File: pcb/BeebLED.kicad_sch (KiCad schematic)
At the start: 13 parts, among them J1 BBC User Port, J2 Jack-DC, U1 74HC14, U2 74LS165, X1 8Mhz

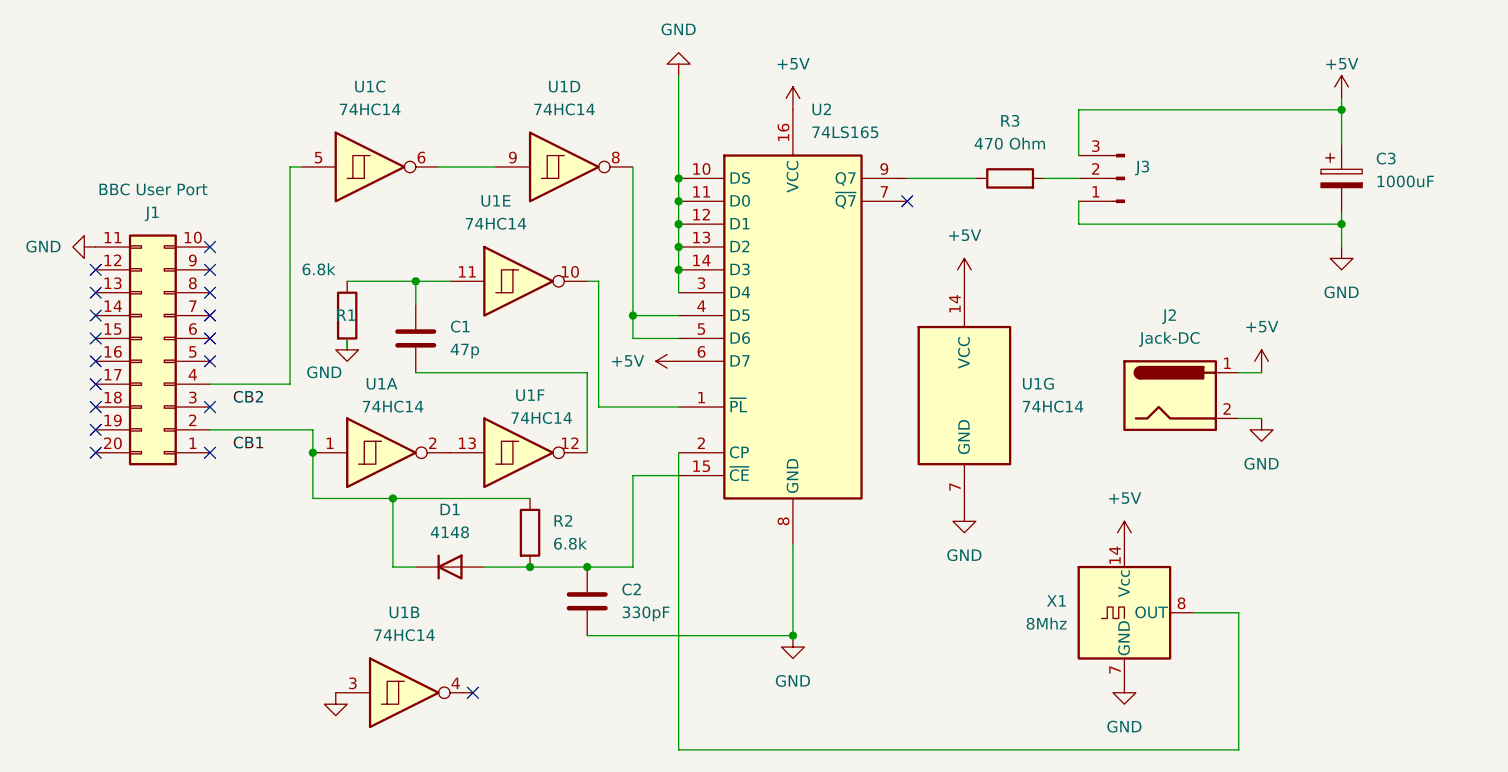
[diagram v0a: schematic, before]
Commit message: Added support for DIP8 crystal
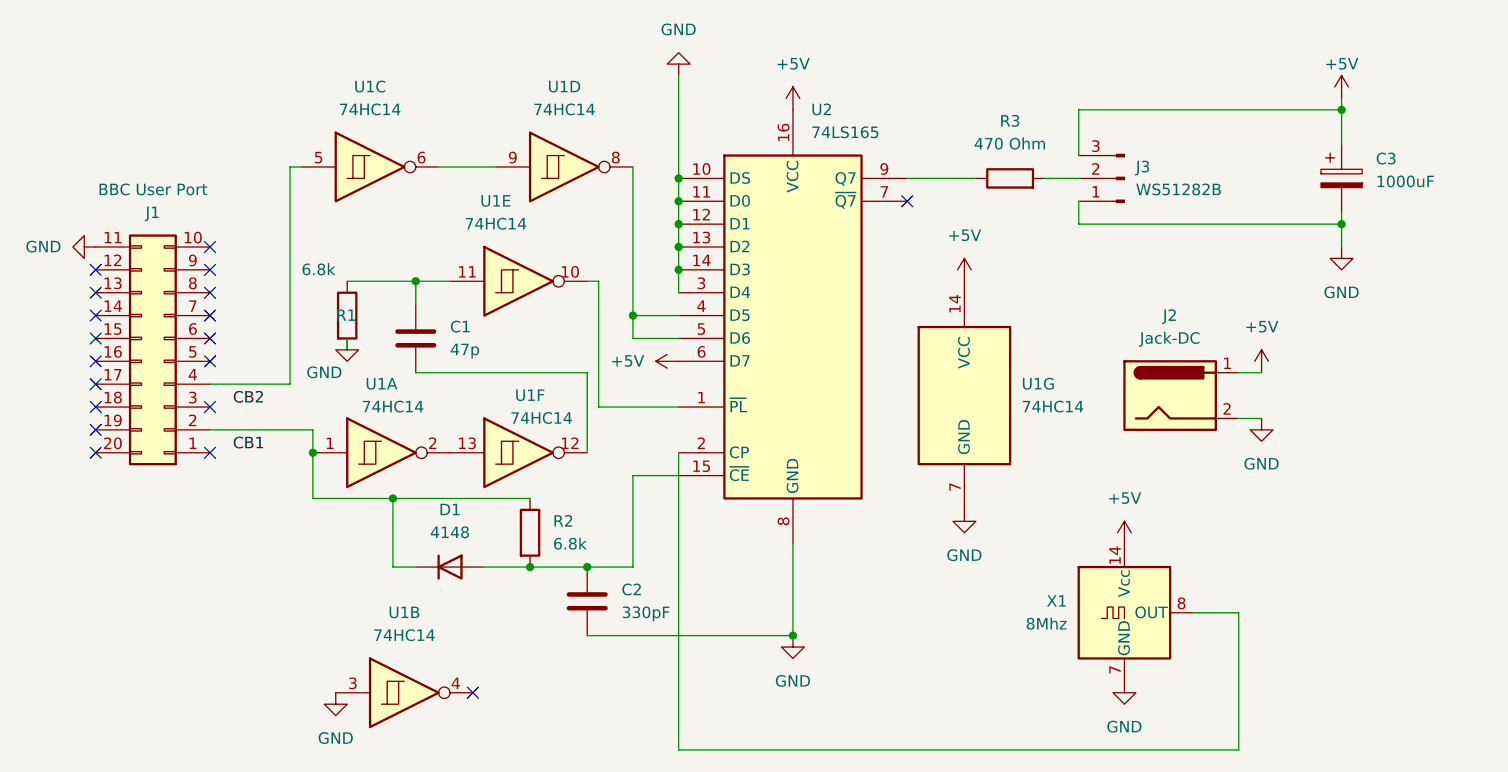
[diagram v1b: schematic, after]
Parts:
- J3: value (none) -> WS51282B; footprint (none) -> Connector_JST:JST_PH_S3B-PH-K_1x03_P2.00mm_Horizontal
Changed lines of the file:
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@@
       (effects (font (size 1.27 1.27)) hide)
     )
-    (property "Value" "" (id 1) (at 102.87 138.43 0))
+    (property "Value" "GND" (id 1) (at 102.87 138.43 0))
     (property "Footprint" "" (id 2) (at 102.87 133.35 0)
       (effects (font (size 1.27 1.27)) hide)
@@
       (effects (font (size 1.27 1.27)) (justify right))
     )
-    (property "Value" "" (id 1) (at 191.77 77.4699 0)
+    (property "Value" "WS51282B" (id 1) (at 191.77 77.4699 0)
       (effects (font (size 1.27 1.27)) (justify right))
     )
-    (property "Footprint" "" (id 2) (at 190.5 76.2 0)
-      (effects (font (size 1.27 1.27)) hide)
-    )
+    (property "Footprint" "Connector_JST:JST_PH_S3B-PH-K_1x03_P2.00mm_Horizontal" (id 2) (at 190.5 76.2 0)
+      (effects (font (size 1.27 1.27)) hide)
+    )

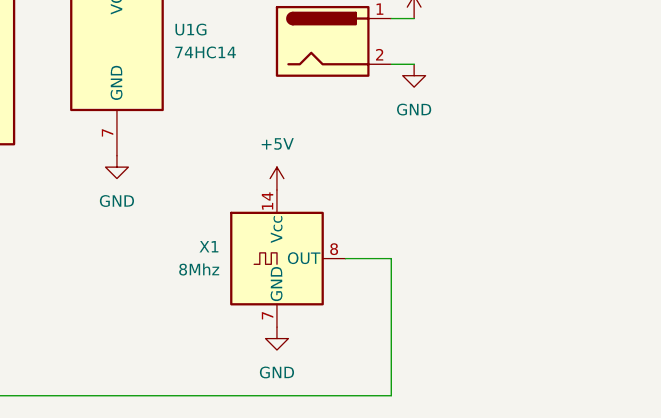
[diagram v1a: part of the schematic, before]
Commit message: Added alternative X2 component to schema and updated PCB
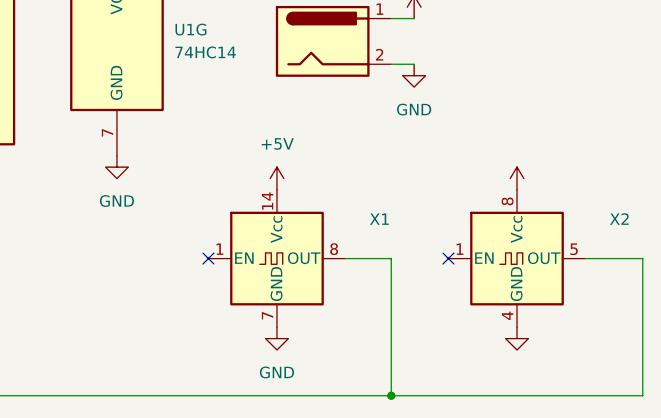
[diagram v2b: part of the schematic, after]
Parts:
- removed X1: 8Mhz, Oscillator:Oscillator_DIP-14, symbol Oscillator:DGOF5S3
- added X1: (no value), symbol Oscillator:CXO_DIP14
- added X2: (no value), symbol Oscillator:CXO_DIP8
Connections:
- net +5V: now also X1.14 (Vcc), X2.8 (Vcc)
- net GND: now also X1.7 (GND), X2.4 (GND)
- net at U2.2 (CP): now also X1.8 (OUT), X2.5 (OUT)
- no-connect marks 19 -> 21
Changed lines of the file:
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@@
   (title_block
     (title "BeebLed")
-    (date "2023-05-05")
-    (rev "v1.0")
+    (date "2023-05-07")
+    (rev "v1.1")
     (company "!FOZ!")
     (comment 1 "Derived from a design on ABNIELSEN.COM")
   )
+  (junction (at 203.2 139.7) (diameter 0) (color 0 0 0 0)
+  )
   (junction (at 100.33 106.68) (diameter 0) (color 0 0 0 0)
   )
@@
   (junction (at 140.97 78.74) (diameter 0) (color 0 0 0 0)
   )
+  (no_connect (at 182.88 124.46))
+  (no_connect (at 209.55 124.46))
   (no_connect (at 76.2 88.9))
   (no_connect (at 88.9 83.82))
@@
     (stroke (width 0) (type default) (color 0 0 0 0))
   )
+  (wire (pts (xy 231.14 124.46) (xy 231.14 139.7))
+    (stroke (width 0) (type default) (color 0 0 0 0))
+  )
   (wire (pts (xy 119.38 119.38) (xy 124.46 119.38))
     (stroke (width 0) (type default) (color 0 0 0 0))
@@
     (stroke (width 0) (type default) (color 0 0 0 0))
   )
+  (wire (pts (xy 203.2 139.7) (xy 231.14 139.7))
+    (stroke (width 0) (type default) (color 0 0 0 0))
+  )
   (wire (pts (xy 140.97 64.77) (xy 140.97 76.2))
     (stroke (width 0) (type default) (color 0 0 0 0))
@@
   )
   (wire (pts (xy 214.63 83.82) (xy 214.63 81.28))
+    (stroke (width 0) (type default) (color 0 0 0 0))
+  )
+  (wire (pts (xy 224.79 124.46) (xy 231.14 124.46))
     (stroke (width 0) (type default) (color 0 0 0 0))
   )
@@
     (pin "7")
   )
+  (symbol (lib_id "Oscillator:CXO_DIP14") (at 190.5 124.46 0) (unit 1)
+    (in_bom yes) (on_board yes) (fields_autoplaced)
+    (property "Reference" "X1" (id 0) (at 201.93 120.1293 0))
+    (property "Value" "" (id 1) (at 201.93 122.6693 0))
+    (property "Footprint" "" (id 2) (at 201.93 133.35 0)
+      (effects (font (size 1.27 1.27)) hide)
+    )
+    (property "Datasheet" "http://cdn-reichelt.de/documents/datenblatt/B400/OSZI.pdf" (id 3) (at 187.96 124.46 0)
+      (effects (font (size 1.27 1.27)) hide)
+    )
+    (pin "1")
+    (pin "14")
+    (pin "7")
+    (pin "8")
+  )
   (symbol (lib_id "power:GND") (at 76.2 83.82 270) (unit 1)
     (in_bom yes) (on_board yes) (fields_autoplaced)
@@
     (pin "1")
   )
+  (symbol (lib_id "power:GND") (at 217.17 132.08 0) (unit 1)
+    (in_bom yes) (on_board yes) (fields_autoplaced)
+    (property "Reference" "#PWR?" (id 0) (at 217.17 138.43 0)
+      (effects (font (size 1.27 1.27)) hide)
+    )
+    (property "Value" "" (id 1) (at 217.17 137.16 0))
+    (property "Footprint" "" (id 2) (at 217.17 132.08 0)
+      (effects (font (size 1.27 1.27)) hide)
+    )
+    (property "Datasheet" "" (id 3) (at 217.17 132.08 0)
+      (effects (font (size 1.27 1.27)) hide)
+    )
+    (pin "1")
+  )
   (symbol (lib_id "Device:C") (at 111.76 93.98 0) (unit 1)
     (in_bom yes) (on_board yes) (fields_autoplaced)
@@
     (pin "7")
   )
+  (symbol (lib_id "power:+5V") (at 217.17 116.84 0) (unit 1)
+    (in_bom yes) (on_board yes) (fields_autoplaced)
+    (property "Reference" "#PWR?" (id 0) (at 217.17 120.65 0)
+      (effects (font (size 1.27 1.27)) hide)
+    )
+    (property "Value" "" (id 1) (at 217.17 111.76 0))
+    (property "Footprint" "" (id 2) (at 217.17 116.84 0)
+      (effects (font (size 1.27 1.27)) hide)
+    )
+    (property "Datasheet" "" (id 3) (at 217.17 116.84 0)
+      (effects (font (size 1.27 1.27)) hide)
+    )
+    (pin "1")
+  )
   (symbol (lib_id "74xx:74LS165") (at 153.67 91.44 0) (unit 1)
     (in_bom yes) (on_board yes) (fields_autoplaced)
@@
     (pin "1")
   )
+  (symbol (lib_id "Oscillator:CXO_DIP8") (at 217.17 124.46 0) (unit 1)
+    (in_bom yes) (on_board yes) (fields_autoplaced)
+    (property "Reference" "X2" (id 0) (at 228.6 120.1293 0))
+    (property "Value" "" (id 1) (at 228.6 122.6693 0))
+    (property "Footprint" "" (id 2) (at 228.6 133.35 0)
+      (effects (font (size 1.27 1.27)) hide)
+    )
+    (property "Datasheet" "http://cdn-reichelt.de/documents/datenblatt/B400/OSZI.pdf" (id 3) (at 214.63 124.46 0)
+      (effects (font (size 1.27 1.27)) hide)
+    )
+    (pin "1")
+    (pin "4")
+    (pin "5")
+    (pin "8")
+  )
   (symbol (lib_id "Device:C") (at 130.81 123.19 0) (unit 1)
     (in_bom yes) (on_board yes) (fields_autoplaced)
@@
     (pin "1")
     (pin "2")
-  )
-  (symbol (lib_id "Oscillator:DGOF5S3") (at 190.5 124.46 0) (unit 1)
-    (in_bom yes) (on_board yes) (fields_autoplaced)
-    (property "Reference" "X1" (id 0) (at 184.15 123.1899 0)
-      (effects (font (size 1.27 1.27)) (justify right))
-    )
-    (property "Value" "8Mhz" (id 1) (at 184.15 125.7299 0)
-      (effects (font (size 1.27 1.27)) (justify right))
-    )
-    (property "Footprint" "Oscillator:Oscillator_DIP-14" (id 2) (at 201.93 133.35 0)
-      (effects (font (size 1.27 1.27)) hide)
-    )
-    (property "Datasheet" "http://www.conwin.com/datasheets/cx/cx030.pdf" (id 3) (at 187.96 124.46 0)
-      (effects (font (size 1.27 1.27)) hide)
-    )
-    (pin "1")
-    (pin "14")
-    (pin "7")
-    (pin "8")
   )
   (symbol (lib_id "power:GND") (at 190.5 132.08 0) (unit 1)
@@
       (reference "#PWR0115") (unit 1) (value "GND") (footprint "")
     )
+    (path "/5c6b7004-a2ee-4e72-af4e-74a84ca656c7"
+      (reference "#PWR?") (unit 1) (value "GND") (footprint "")
+    )
+    (path "/677eb441-07e4-425e-8392-d8213b082473"
+      (reference "#PWR?") (unit 1) (value "+5V") (footprint "")
+    )
     (path "/65ed6649-7f77-42ba-8364-96e8d5d3ec59"
       (reference "C1") (unit 1) (value "47p") (footprint "Capacitor_THT:C_Disc_D5.0mm_W2.5mm_P2.50mm")
@@
       (reference "U2") (unit 1) (value "74LS165") (footprint "Package_DIP:DIP-16_W7.62mm_Socket")
     )
-    (path "/a0f7df33-f242-4a57-b335-8b5bb3325289"
+    (path "/448458c6-28d1-4ce1-90d2-c1c26c74c093"
       (reference "X1") (unit 1) (value "8Mhz") (footprint "Oscillator:Oscillator_DIP-14")
     )
-  )
+    (path "/826a22b3-cf90-4ca6-806d-060835b51dd9"
+      (reference "X2") (unit 1) (value "8Mhz") (footprint "Oscillator:Oscillator_DIP-8")
+    )
+  )
